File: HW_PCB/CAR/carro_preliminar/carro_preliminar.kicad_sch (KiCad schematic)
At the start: 25 parts, among them J1 V_Battery, J2 STLINK, J3 Puente H, J4 Puente_H2, J5 UART, J6 Servo_Motor, J7 NRF24_Con, SW1 SW_DPST_x2, U1 STM32F103C8Tx, U2 AMS1117-3.3, Y1 8MHz

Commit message: Carrito pcb, 25-02-26
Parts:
- removed J3: Puente H, Connector_PinHeader_2.54mm:PinHeader_1x08_P2.54mm_Vertical, symbol Connector_Generic:Conn_01x08
- removed J4: Puente_H2, Connector_PinHeader_2.54mm:PinHeader_1x08_P2.54mm_Vertical, symbol Connector_Generic:Conn_01x08
- added C10, C12: 100nF, Capacitor_SMD:C_0805_2012Metric_Pad1.18x1.45mm_HandSolder, symbol Device:C
- added C11, C13: 10uF, Capacitor_SMD:C_0805_2012Metric_Pad1.18x1.45mm_HandSolder, symbol Device:C
- added C1_Driver1, C2_driver1: 0.1uF, Capacitor_SMD:C_0805_2012Metric, symbol Device:C
- added C3_Driver1: TAJB226K016RNJ_10uF, TAJB226K016RNJ:CAPPC3528X210N, symbol TAJB226K016RNJ:TAJB226K016RNJ
- added IC1: TB6612FNG, Package_SO:SSOP-24_5.3x8.2mm_P0.65mm, symbol TB6612FNG:TB6612FNG
- added J3: Motores, Connector_PinHeader_2.54mm:PinHeader_1x04_P2.54mm_Vertical, symbol Connector_Generic:Conn_01x04
- added U3: AMS1117-3.3, Package_TO_SOT_SMD:SOT-223-3_TabPin2, symbol Regulator_Linear:AMS1117-3.3
- added U4: LM1117DT-5.0, Package_TO_SOT_SMD:TO-252-3_TabPin2, symbol Regulator_Linear:LM1117DT-5.0
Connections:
- net CE is gone; now on net PA10: J7.2 (Pin_2)
- net CNS is gone; now on net PA8: J7.7 (Pin_7)
- net IRQ is gone; now on net PA9: J7.5 (Pin_5)
- net MISO is gone; now on net PB14: J7.4 (Pin_4)
- net MOSI is gone; now on net PB15: J7.6 (Pin_6)
- net PWM is gone; now on net PB5: J6.1 (Pin_1)
- net Rx is gone; now on net PB11: J5.2 (Pin_2)
- net SCK is gone; now on net PB13: J7.3 (Pin_3)
- net Tx is gone; now on net PB10: J5.1 (Pin_1)
- net A01: now also IC1.1 (AO1), IC1.2 (AO1'), J3.4 (Pin_4)
- net A02: now also IC1.5 (AO2), IC1.6 (AO2'), J3.3 (Pin_3)
- net B01: now also IC1.7 (BO2), IC1.8 (BO2'), J3.2 (Pin_2)
- net B02: now also IC1.11 (BO1), IC1.12 (BO1'), J3.1 (Pin_1)
- net GND: now also C10.2, C11.2, C12.2, C13.2, C1_Driver1.2, C2_driver1.2, C3_Driver1.1, IC1.10 (PGND2'), IC1.18 (GND), IC1.3 (PGND1), IC1.4 (PGND1'), IC1.9 (PGND2), U3.1 (GND)
- net PA0: now also IC1.23 (PWMA)
- net PA1: now also IC1.15 (PWMB)
- net PA3: now also IC1.21 (AIN1)
- net PA4: now also IC1.22 (AIN2)
- net PA5: now also IC1.17 (BIN1)
- net PA6: now also IC1.16 (BIN2)
- net PC13: no longer R3.1
- net VCC: now also C2_driver1.1, IC1.19 (STBY), IC1.20 (VCC); no longer J7.8 (Pin_8)
- net VIN: now also C12.1, C13.1, C1_Driver1.1, C3_Driver1.2, IC1.13 (VM2), IC1.14 (VM3), IC1.24 (VM1), U3.3 (VI)
- new net VCC_nrf24l01: C10.1, C11.1, J7.8 (Pin_8), R3.1, U3.2 (VO)
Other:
- moved on the sheet: J5, J6, J7

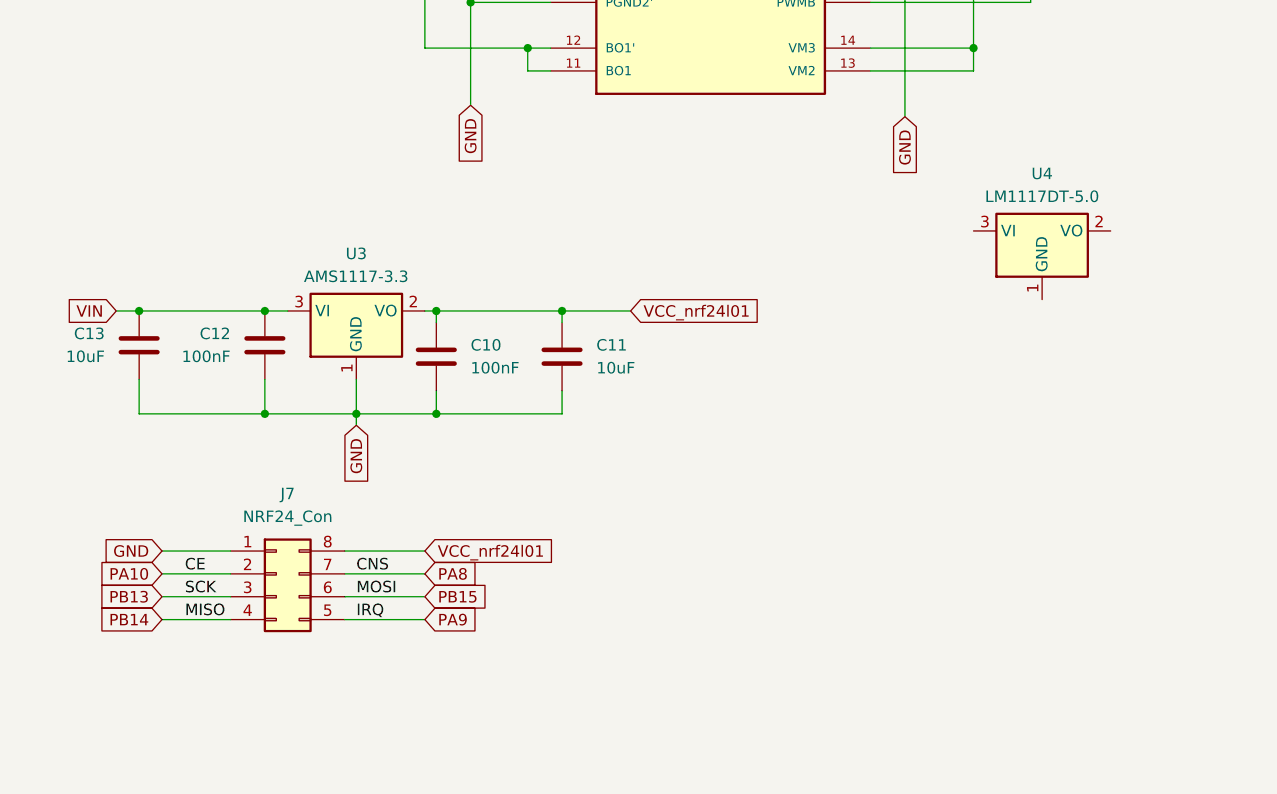
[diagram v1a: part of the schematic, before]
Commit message: added an advance for the CAR PCB
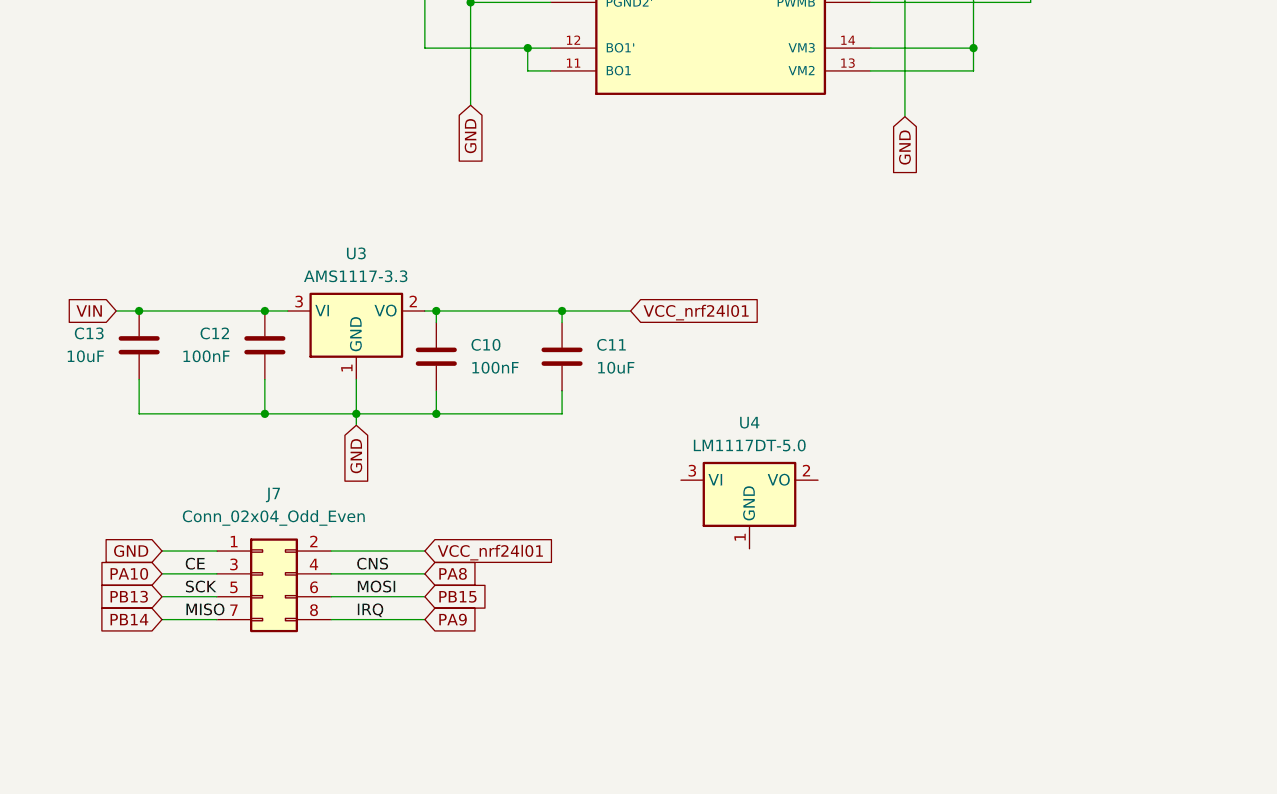
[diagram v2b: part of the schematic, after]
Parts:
- removed J7: NRF24_Con, Connector_PinHeader_2.54mm:PinHeader_2x04_P2.54mm_Vertical, symbol Connector_Generic:Conn_02x04_Counter_Clockwise
- added J7: Conn_02x04_Odd_Even, Connector_PinHeader_2.54mm:PinHeader_2x04_P2.54mm_Vertical, symbol Connector_Generic:Conn_02x04_Odd_Even
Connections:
- net GND: now also J7.1 (Pin_1)
- net PA10: now also J7.3 (Pin_3)
- net PA8: now also J7.4 (Pin_4)
- net PA9: now also J7.8 (Pin_8)
- net PB13: now also J7.5 (Pin_5)
- net PB14: now also J7.7 (Pin_7)
- net PB15: now also J7.6 (Pin_6)
- net VCC_nrf24l01: now also J7.2 (Pin_2)
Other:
- moved on the sheet: U4
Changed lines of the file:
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@@
 	(wire
 		(pts
+			(xy 150.876 148.59) (xy 161.29 148.59)
+		)
+		(stroke
+			(width 0)
+			(type default)
+		)
+	)
+	(wire
+		(pts
 			(xy 22.86 55.88) (xy 16.51 55.88)
 		)
@@
 	(wire
 		(pts
+			(xy 150.876 153.67) (xy 161.29 153.67)
+		)
+		(stroke
+			(width 0)
+			(type default)
+		)
+	)
+	(wire
+		(pts
 			(xy 222.25 22.86) (xy 222.25 52.07)
 		)
@@
 	(wire
 		(pts
-			(xy 132.08 148.59) (xy 139.7 148.59)
+			(xy 132.08 148.59) (xy 138.176 148.59)
 		)
 		(stroke
@@
 	(wire
 		(pts
-			(xy 152.4 146.05) (xy 161.29 146.05)
-		)
-		(stroke
-			(width 0)
-			(type default)
-		)
-	)
-	(wire
-		(pts
 			(xy 99.06 88.9) (xy 96.52 88.9)
 		)
@@
 	(wire
 		(pts
-			(xy 132.08 146.05) (xy 139.7 146.05)
+			(xy 132.08 146.05) (xy 138.176 146.05)
 		)
 		(stroke
@@
 	(wire
 		(pts
-			(xy 152.4 153.67) (xy 161.29 153.67)
-		)
-		(stroke
-			(width 0)
-			(type default)
-		)
-	)
-	(wire
-		(pts
 			(xy 194.31 25.4) (xy 194.31 22.86)
 		)
@@
 	(wire
 		(pts
-			(xy 132.08 153.67) (xy 139.7 153.67)
+			(xy 132.08 153.67) (xy 138.176 153.67)
 		)
 		(stroke
@@
 	(wire
 		(pts
-			(xy 132.08 151.13) (xy 139.7 151.13)
+			(xy 132.08 151.13) (xy 138.176 151.13)
 		)
 		(stroke
@@
 	(wire
 		(pts
+			(xy 150.876 151.13) (xy 161.29 151.13)
+		)
+		(stroke
+			(width 0)
+			(type default)
+		)
+	)
+	(wire
+		(pts
+			(xy 150.876 146.05) (xy 161.29 146.05)
+		)
+		(stroke
+			(width 0)
+			(type default)
+		)
+	)
+	(wire
+		(pts
 			(xy 71.12 57.15) (xy 83.82 57.15)
 		)
@@
 	(wire
 		(pts
-			(xy 152.4 151.13) (xy 161.29 151.13)
-		)
-		(stroke
-			(width 0)
-			(type default)
-		)
-	)
-	(wire
-		(pts
 			(xy 166.37 59.69) (xy 166.37 62.23)
 		)
@@
 	(wire
 		(pts
-			(xy 152.4 148.59) (xy 161.29 148.59)
-		)
-		(stroke
-			(width 0)
-			(type default)
-		)
-	)
-	(wire
-		(pts
 			(xy 167.64 66.04) (xy 167.64 67.31)
 		)
@@
 	(symbol
 		(lib_id "Regulator_Linear:LM1117DT-5.0")
-		(at 229.87 110.49 0)
+		(at 197.358 138.176 0)
 		(unit 1)
 		(exclude_from_sim no)
@@
 		(fields_autoplaced yes)
 		(property "Reference" "U4"
-			(at 229.87 104.14 0)
+			(at 197.358 131.826 0)
 			(effects
 				(font
@@
 		)
 		(property "Value" "LM1117DT-5.0"
-			(at 229.87 106.68 0)
+			(at 197.358 134.366 0)
 			(effects
 				(font
@@
 		)
 		(property "Footprint" "Package_TO_SOT_SMD:TO-252-3_TabPin2"
-			(at 229.87 110.49 0)
+			(at 197.358 138.176 0)
 			(effects
 				(font
@@
 		)
 		(property "Datasheet" "http://www.ti.com/lit/ds/symlink/lm1117.pdf"
-			(at 229.87 110.49 0)
+			(at 197.358 138.176 0)
 			(effects
 				(font
@@
 		)
 		(property "Description" "800mA Low-Dropout Linear Regulator, 5.0V fixed output, TO-252"
-			(at 229.87 110.49 0)
+			(at 197.358 138.176 0)
 			(effects
 				(font
@@
 	)
 	(symbol
-		(lib_id "Connector_Generic:Conn_02x04_Counter_Clockwise")
-		(at 144.78 148.59 0)
+		(lib_id "Device:C")
+		(at 63.5 72.39 180)
 		(unit 1)
 		(exclude_from_sim no)
@@
 		(dnp no)
 		(fields_autoplaced yes)
-		(property "Reference" "J7"
-			(at 146.05 139.7 0)
+		(property "Reference" "C1"
+			(at 67.31 71.1199 0)
 			(effects
 				(font
 					(size 1.27 1.27)
 				)
+				(justify right)
 			)
 		)
-		(property "Value" "NRF24_Con"
-			(at 146.05 142.24 0)
+		(property "Value" "1uF"
+			(at 67.31 73.6599 0)
 			(effects
 				(font
 					(size 1.27 1.27)
 				)
+				(justify right)
 			)
 		)
-		(property "Footprint" "Connector_PinHeader_2.54mm:PinHeader_2x04_P2.54mm_Vertical"
-			(at 144.78 148.59 0)
+		(property "Footprint" "Capacitor_SMD:C_0805_2012Metric"
+			(at 62.5348 68.58 0)
 			(effects
 				(font
@@
 		)
 		(property "Datasheet" "~"
-			(at 144.78 148.59 0)
+			(at 63.5 72.39 0)
 			(effects
 				(font
@@
 			)
 		)
-		(property "Description" "Generic connector, double row, 02x04, counter clockwise pin numbering scheme (similar to DIP package numbering), script generated (kicad-library-utils/schlib/autogen/connector/)"
-			(at 144.78 148.59 0)
+		(property "Description" "Unpolarized capacitor"
+			(at 63.5 72.39 0)
 			(effects
 				(font
@@
 			)
 		)
-		(pin "3"
-		)
-		(pin "5"
-		)
-		(pin "4"
-		)
 		(pin "1"
 		)
 		(pin "2"
 		)
-		(pin "6"
-		)
-		(pin "8"
-		)
-		(pin "7"
-		)
 		(instances
-			(project ""
+			(project "carro_preliminar"
 				(path "/b44e6fd1-366d-4904-8da1-e136aff2ec70"
-					(reference "J7")
+					(reference "C1")
 					(unit 1)
 				)
@@
 	)
 	(symbol
-		(lib_id "Device:C")
-		(at 63.5 72.39 180)
+		(lib_id "Device:Crystal")
+		(at 78.74 33.02 90)
 		(unit 1)
 		(exclude_from_sim no)
@@
 		(dnp no)
 		(fields_autoplaced yes)
-		(property "Reference" "C1"
-			(at 67.31 71.1199 0)
+		(property "Reference" "Y1"
+			(at 82.55 31.7499 90)
 			(effects
 				(font
@@
 			)
 		)
-		(property "Value" "1uF"
-			(at 67.31 73.6599 0)
+		(property "Value" "8MHz"
+			(at 82.55 34.2899 90)
 			(effects
 				(font
@@
 			)
 		)
-		(property "Footprint" "Capacitor_SMD:C_0805_2012Metric"
-			(at 62.5348 68.58 0)
+		(property "Footprint" "Crystal:Crystal_HC52-U_Vertical"
+			(at 78.74 33.02 0)
 			(effects
 				(font
@@
 		)
 		(property "Datasheet" "~"
-			(at 63.5 72.39 0)
+			(at 78.74 33.02 0)
 			(effects
 				(font
@@
 			)
 		)
-		(property "Description" "Unpolarized capacitor"
-			(at 63.5 72.39 0)
+		(property "Description" "Two pin crystal"
+			(at 78.74 33.02 0)
 			(effects
 				(font
@@
 			(project "carro_preliminar"
 				(path "/b44e6fd1-366d-4904-8da1-e136aff2ec70"
-					(reference "C1")
+					(reference "Y1")
 					(unit 1)
 				)
@@
 	)
 	(symbol
-		(lib_id "Device:Crystal")
-		(at 78.74 33.02 90)
+		(lib_id "Regulator_Linear:AMS1117-3.3")
+		(at 83.82 49.53 0)
 		(unit 1)
 		(exclude_from_sim no)
@@
 		(dnp no)
 		(fields_autoplaced yes)
-		(property "Reference" "Y1"
-			(at 82.55 31.7499 90)
+		(property "Reference" "U2"
+			(at 83.82 43.18 0)
 			(effects
 				(font
 					(size 1.27 1.27)
 				)
-				(justify right)
 			)
 		)
-		(property "Value" "8MHz"
-			(at 82.55 34.2899 90)
+		(property "Value" "AMS1117-3.3"
+			(at 83.82 45.72 0)
 			(effects
 				(font
 					(size 1.27 1.27)
 				)
-				(justify right)
 			)
 		)
-		(property "Footprint" "Crystal:Crystal_HC52-U_Vertical"
-			(at 78.74 33.02 0)
+		(property "Footprint" "Package_TO_SOT_SMD:SOT-223-3_TabPin2"
+			(at 83.82 44.45 0)
 			(effects
 				(font
@@
 			)
 		)
-		(property "Datasheet" "~"
-			(at 78.74 33.02 0)
+		(property "Datasheet" "http://www.advanced-monolithic.com/pdf/ds1117.pdf"
+			(at 86.36 55.88 0)
 			(effects
 				(font
@@
 			)
 		)
-		(property "Description" "Two pin crystal"
-			(at 78.74 33.02 0)
+		(property "Description" "1A Low Dropout regulator, positive, 3.3V fixed output, SOT-223"
+			(at 83.82 49.53 0)
 			(effects
 				(font
@@
 			)
 		)
+		(pin "3"
+		)
 		(pin "1"
 		)
@@
 			(project "carro_preliminar"
 				(path "/b44e6fd1-366d-4904-8da1-e136aff2ec70"
-					(reference "Y1")
+					(reference "U2")
 					(unit 1)
 				)
@@
 	)
 	(symbol
-		(lib_id "Regulator_Linear:AMS1117-3.3")
-		(at 83.82 49.53 0)
+		(lib_id "Connector_Generic:Conn_02x04_Odd_Even")
+		(at 143.256 148.59 0)
 		(unit 1)
 		(exclude_from_sim no)
@@
 		(dnp no)
 		(fields_autoplaced yes)
-		(property "Reference" "U2"
-			(at 83.82 43.18 0)
+		(property "Reference" "J7"
+			(at 144.526 139.7 0)
 			(effects
 				(font
@@
 			)
 		)
-		(property "Value" "AMS1117-3.3"
-			(at 83.82 45.72 0)
+		(property "Value" "Conn_02x04_Odd_Even"
+			(at 144.526 142.24 0)
 			(effects
 				(font
@@
 			)
 		)
-		(property "Footprint" "Package_TO_SOT_SMD:SOT-223-3_TabPin2"
-			(at 83.82 44.45 0)
+		(property "Footprint" "Connector_PinHeader_2.54mm:PinHeader_2x04_P2.54mm_Vertical"
+			(at 143.256 148.59 0)
 			(effects
 				(font
@@
 			)
 		)
-		(property "Datasheet" "http://www.advanced-monolithic.com/pdf/ds1117.pdf"
-			(at 86.36 55.88 0)
+		(property "Datasheet" "~"
+			(at 143.256 148.59 0)
 			(effects
 				(font
@@
 			)
 		)
-		(property "Description" "1A Low Dropout regulator, positive, 3.3V fixed output, SOT-223"
-			(at 83.82 49.53 0)
+		(property "Description" "Generic connector, double row, 02x04, odd/even pin numbering scheme (row 1 odd numbers, row 2 even numbers), script generated (kicad-library-utils/schlib/autogen/connector/)"
+			(at 143.256 148.59 0)
 			(effects
 				(font
@@
 			)
 		)
+		(pin "5"
+		)
+		(pin "7"
+		)
 		(pin "3"
 		)
+		(pin "2"
+		)
 		(pin "1"
 		)
-		(pin "2"
+		(pin "4"
+		)
+		(pin "8"
+		)
+		(pin "6"
 		)
 		(instances
-			(project "carro_preliminar"
+			(project ""
 				(path "/b44e6fd1-366d-4904-8da1-e136aff2ec70"
-					(reference "U2")
+					(reference "J7")
 					(unit 1)
 				)

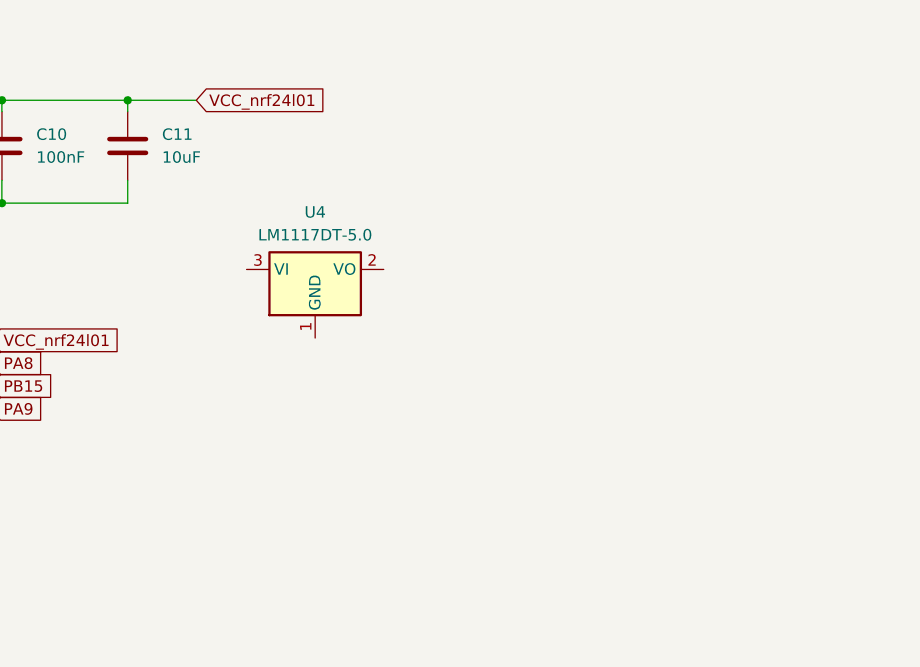
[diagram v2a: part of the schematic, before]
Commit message: Placa de carro terminada al menos preliminarmente
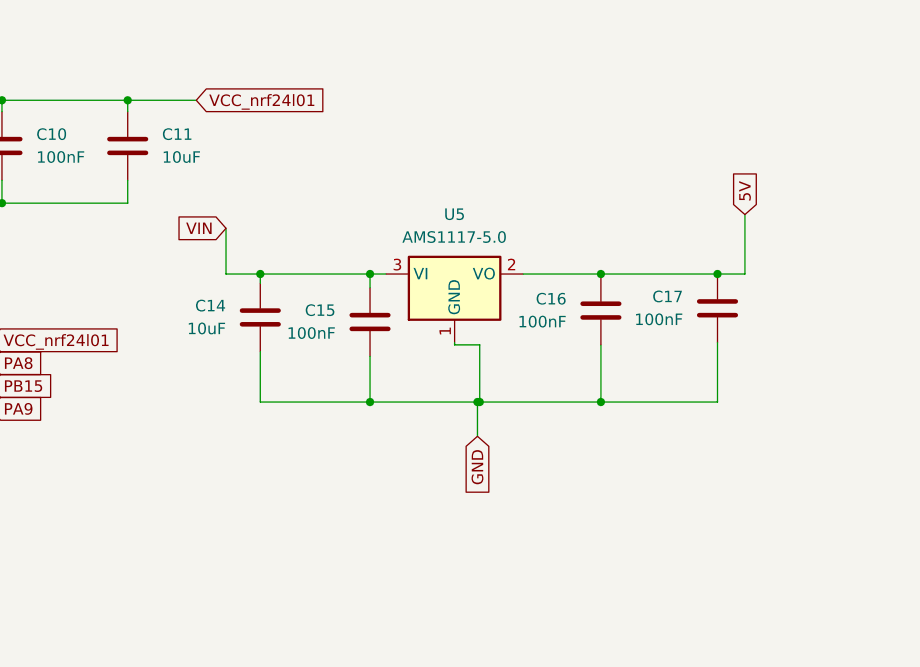
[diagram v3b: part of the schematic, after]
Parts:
- removed U4: LM1117DT-5.0, Package_TO_SOT_SMD:TO-252-3_TabPin2, symbol Regulator_Linear:LM1117DT-5.0
- added C14: 10uF, Capacitor_SMD:C_0805_2012Metric_Pad1.18x1.45mm_HandSolder, symbol Device:C
- added C15, C16, C17: 100nF, Capacitor_SMD:C_0805_2012Metric_Pad1.18x1.45mm_HandSolder, symbol Device:C
- added U5: AMS1117-5.0, Package_TO_SOT_SMD:SOT-223-3_TabPin2, symbol Regulator_Linear:AMS1117-5.0
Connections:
- net 5V: now also C16.1, C17.1, U5.2 (VO)
- net GND: now also C14.2, C15.2, C16.2, C17.2, U5.1 (GND)
- net VIN: now also C14.1, C15.1, U5.3 (VI)
